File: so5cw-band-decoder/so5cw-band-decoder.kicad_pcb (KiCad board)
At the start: 2 copper layers, 140 x 154 mm, 136 parts, among them J1 DA15_Receptacle, J2 AudioJack3_SwitchTR, J3 Barrel_Jack_MountingPin, J4 RJ45, K1 TIANBO-HJR-4102-L, K10 TIANBO-HJR-4102-L, K11 TIANBO-HJR-4102-L, K12 TIANBO-HJR-4102-L, K2 TIANBO-HJR-4102-L, K3 TIANBO-HJR-4102-L, K4 TIANBO-HJR-4102-L, K5 TIANBO-HJR-4102-L, K6 TIANBO-HJR-4102-L, K7 TIANBO-HJR-4102-L, K8 TIANBO-HJR-4102-L, K9 TIANBO-HJR-4102-L, Q1 BS170F, Q2 BS170F, Q3 BS170F, Q4 BS170F, SW1 TASTER 3305D, SW2 TASTER 3305D, SW3 TASTER 3305D, SW4 TASTER 3305D, SW5 SW_Omron_B3FS, U1 RaspberryPi_Pico, U2 ULN2003A, U3 ULN2003A, U4 LM78M05_TO220

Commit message: Rearrange parts and route the critical connections. Needs cleanup.
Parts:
- C1, C10, C11, C12, C13, C14, C15, C16, C17, C18, C19, C2, C20, C21, C22, C23, C24, C3, C4, C5, C6, C7, C8, C9, R33: moved to B.Cu
- moved C30 90.7 mm to (148.6, 49.5)
- moved C31 87.2 mm to (148.3, 56.1)
- moved K1 84.6 mm to (46.0, 137.7)
- moved C29 82.6 mm to (81.5, 29.5), turned to 90 degrees
- moved K2 69.3 mm to (46.0, 121.9)
- moved K12 68.2 mm to (96.5, 150.4), turned to 180 degrees
- moved R17 68.0 mm to (101.2, 26.4), turned to 180 degrees
- moved R18 67.2 mm to (101.3, 29.0), turned to 180 degrees
- moved R19 65.9 mm to (123.7, 158.8), turned to 90 degrees
- moved K11 65.3 mm to (96.5, 134.9), turned to 180 degrees
- moved K3 56.7 mm to (46.0, 106.2)
- moved K10 53.6 mm to (96.5, 119.1), turned to 180 degrees
- moved K8 53.5 mm to (96.5, 87.9), turned to 180 degrees
- moved C6 51.7 mm to (73.2, 75.2)
- moved C5 50.1 mm to (71.4, 75.2)
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- renumbered K8 to K10, K10 to K11, K9 to K8, K11 to K9
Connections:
- R1 pad 2: /R1A -> /R1F
- R10 pad 2: /R2D -> /R2C
- R11 pad 2: /R2E -> /R2B
- R12 pad 2: /R2F -> /R2A
- R2 pad 2: /R1B -> /R1E
- R3 pad 2: /R1C -> /R1D
- R4 pad 2: /R1D -> /R1C
- R5 pad 2: /R1E -> /R1B
- R6 pad 2: /R1F -> /R1A
- R7 pad 2: /R2A -> /R2F
- R8 pad 2: /R2B -> /R2E
- R9 pad 2: /R2C -> /R2D
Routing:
- net +12V: track 0.00 -> 196.7 mm
- net /R2AR: track 0.00 -> 187.3 mm
- net /SW1: track 0.00 -> 175.2 mm
- net /SW2: track 0.00 -> 169.0 mm
- net /R1AR: track 0.00 -> 159.4 mm, vias 0 -> 1
- net /R2BR: track 0.00 -> 151.7 mm
- net /R1BR: track 0.00 -> 149.6 mm, vias 0 -> 1
- net /R1FR: track 0.00 -> 137.3 mm, vias 0 -> 1
- net /R1CR: track 0.00 -> 135.1 mm, vias 0 -> 1
- net /R2FP: track 0.00 -> 123.8 mm
- net /R1DR: track 0.00 -> 123.7 mm, vias 0 -> 1
- net /SW4: track 0.00 -> 121.6 mm
- net /R1ER: track 0.00 -> 119.3 mm, vias 0 -> 1
- net /R2CR: track 0.00 -> 117.6 mm
- net /SW3: track 0.00 -> 115.9 mm
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
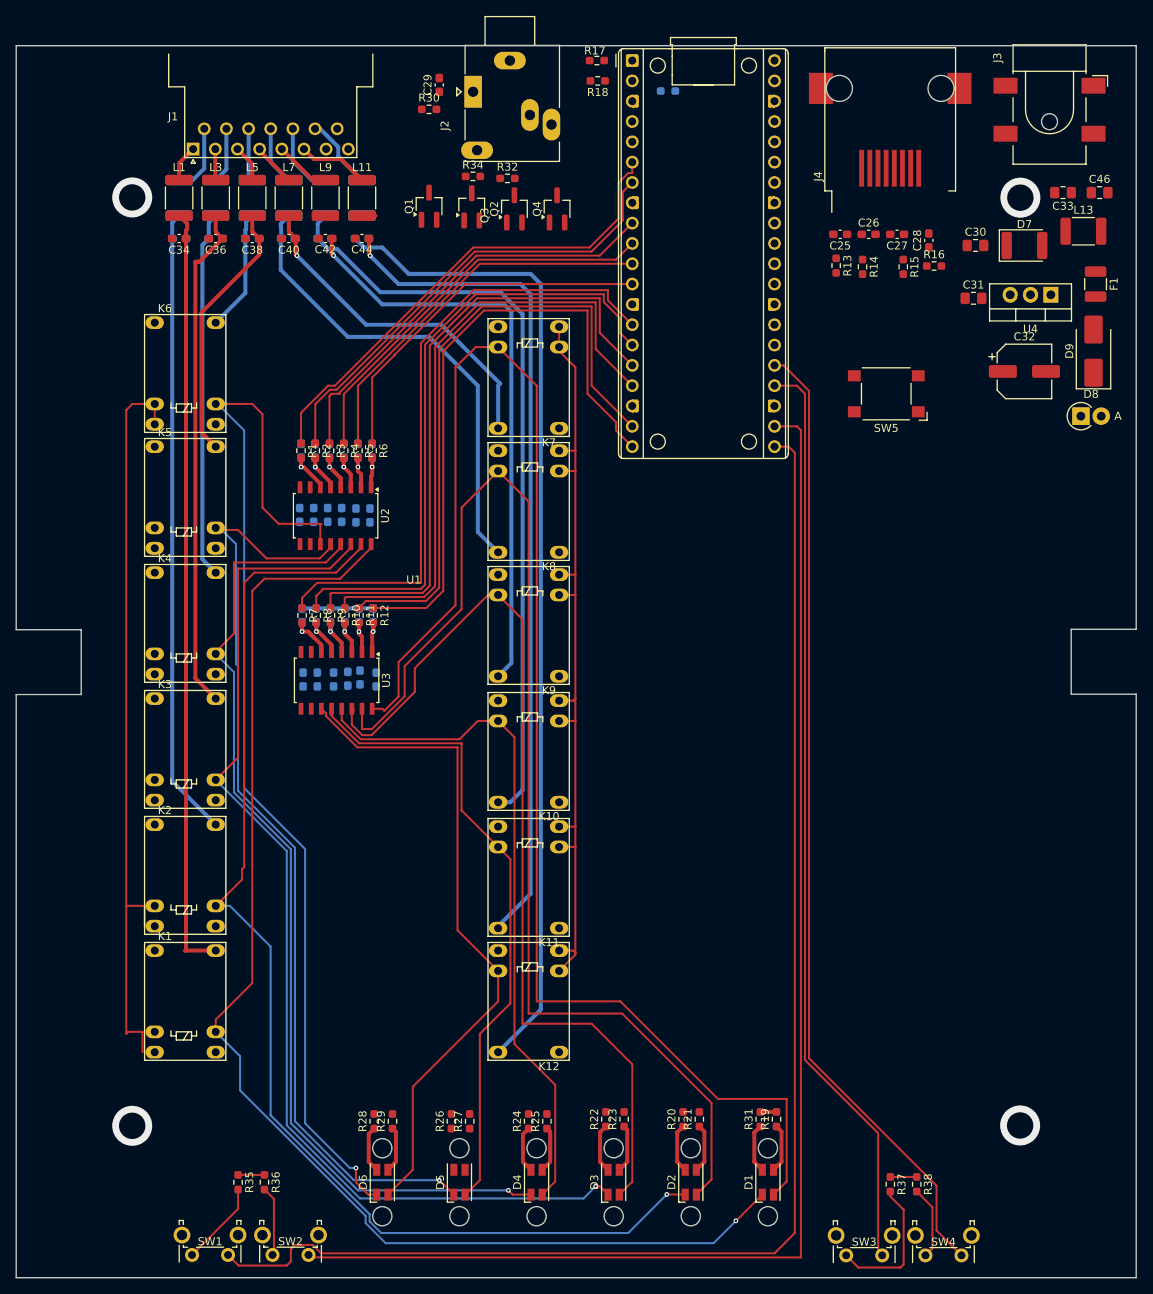
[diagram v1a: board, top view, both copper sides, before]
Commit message: some more routing, add buzzer, heatsink for 5V reg, etc.
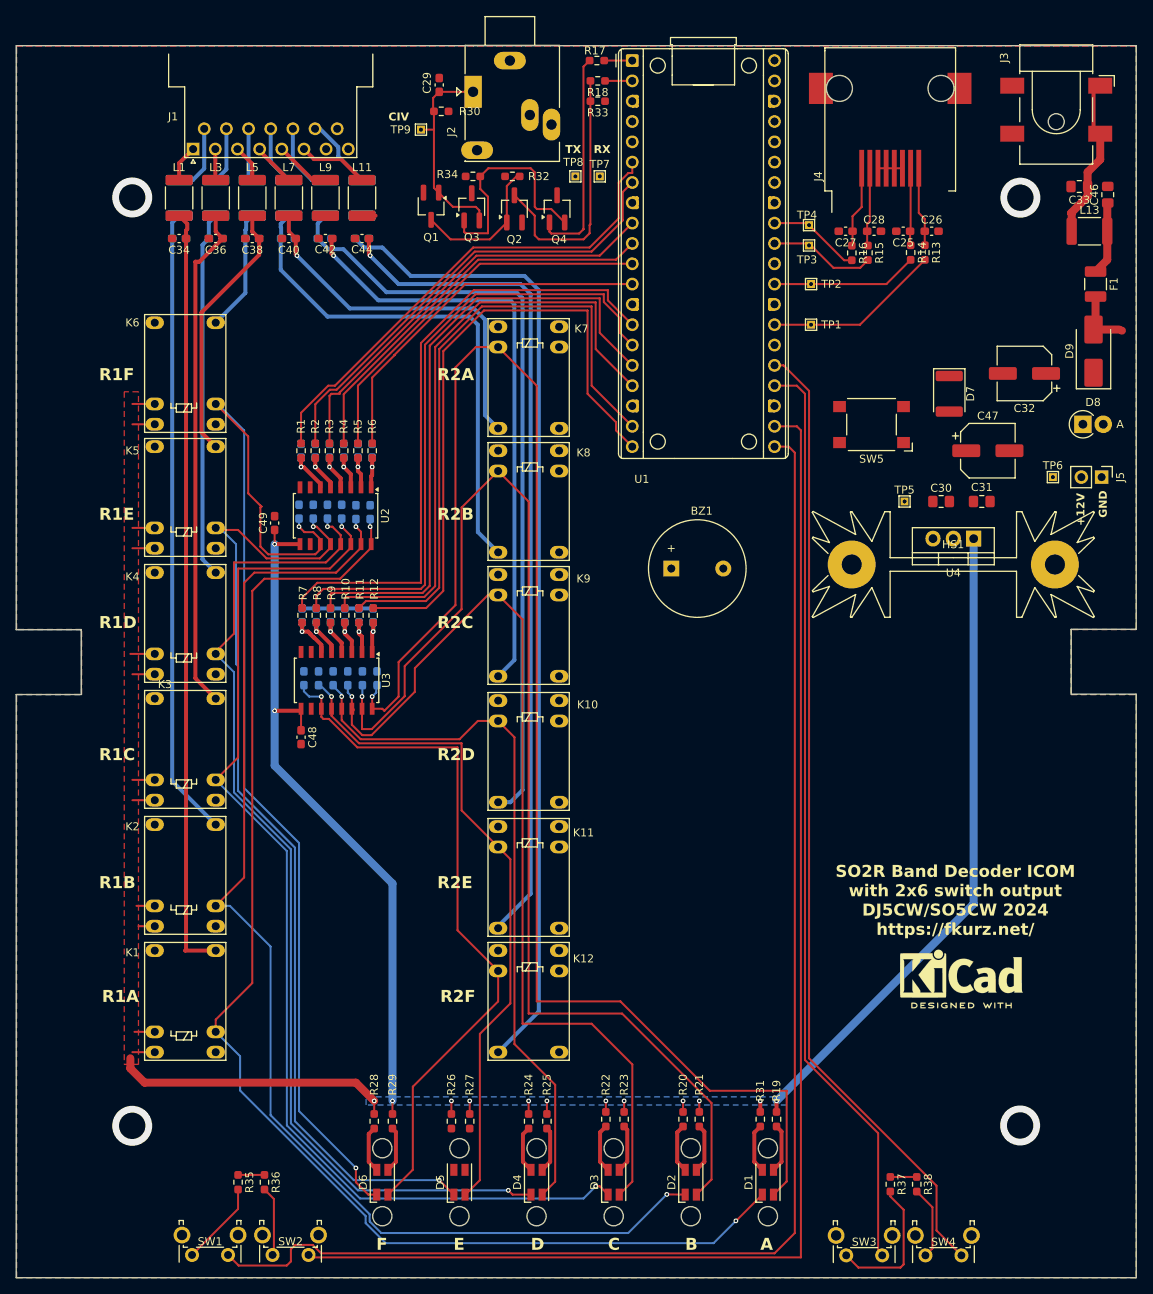
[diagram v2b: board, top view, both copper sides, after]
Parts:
- added BZ1: Buzzer, so5cw-band-decoder-components:Buzzer_12x9.5RM6.5, F.Cu at (110.5, 89.9)
- added C47: 47u, Capacitor_SMD:CP_Elec_6.3x7.7, F.Cu at (150.1, 75.2)
- added C48: 100n, Capacitor_SMD:C_0603_1608Metric_Pad1.08x0.95mm_HandSolder, F.Cu at (64.3, 111.0)
- added C49: 100n, Capacitor_SMD:C_0603_1608Metric_Pad1.08x0.95mm_HandSolder, F.Cu at (61.0, 84.2)
- added FID1: KiCad Logo, Symbol:KiCad-Logo2_6mm_SilkScreen, F.Cu at (146.8, 140.5)
- added HS1: Heatsink_Pad, Heatsink:Heatsink_Fischer_SK104-STC-STIC_35x13mm_2xDrill2.5mm, F.Cu at (145.8, 89.4)
- added J5: Conn_01x02_Pin, Connector_PinHeader_2.54mm:PinHeader_1x02_P2.54mm_Vertical, F.Cu at (164.3, 78.5)
- added TP1: TestPoint, TestPoint:TestPoint_THTPad_1.0x1.0mm_Drill0.5mm, F.Cu at (128.0, 59.4)
- added TP2: TestPoint, TestPoint:TestPoint_THTPad_1.0x1.0mm_Drill0.5mm, F.Cu at (128.0, 54.4)
- added TP3: TestPoint, TestPoint:TestPoint_THTPad_1.0x1.0mm_Drill0.5mm, F.Cu at (127.8, 49.5)
- added TP4: TestPoint, TestPoint:TestPoint_THTPad_1.0x1.0mm_Drill0.5mm, F.Cu at (127.8, 47.0)
- added TP5: TestPoint, TestPoint:TestPoint_THTPad_1.0x1.0mm_Drill0.5mm, F.Cu at (139.7, 81.5)
- added TP6: TestPoint, TestPoint:TestPoint_THTPad_1.0x1.0mm_Drill0.5mm, F.Cu at (158.2, 78.5)
- added TP7: TestPoint, TestPoint:TestPoint_THTPad_1.0x1.0mm_Drill0.5mm, F.Cu at (101.6, 40.9)
- added TP8: TestPoint, TestPoint:TestPoint_THTPad_1.0x1.0mm_Drill0.5mm, F.Cu at (98.6, 40.9)
- added TP9: TestPoint, TestPoint:TestPoint_THTPad_1.0x1.0mm_Drill0.5mm, F.Cu at (79.2, 35.1)
- J3: value Barrel_Jack_MountingPin -> Barrel_Jack
- R33: moved to F.Cu
- moved C30 32.3 mm to (144.3, 81.5)
- moved U4 32.0 mm to (148.3, 86.2)
- moved C31 25.4 mm to (149.4, 81.5)
- moved D7 20.8 mm to (145.3, 68.1), turned to -90 degrees
- moved R13 11.2 mm to (142.2, 50.4)
- moved R16 10.4 mm to (133.1, 50.5), turned to -90 degrees
- moved R33 8.88 mm to (101.3, 31.5)
- moved C26 7.88 mm to (143.1, 47.8)
- moved C25 7.88 mm to (139.5, 47.8)
- moved C28 6.94 mm to (135.9, 47.8), turned to 0 degrees
- moved C27 6.45 mm to (132.3, 47.8)
- moved R14 6.27 mm to (140.5, 50.4)
- moved R15 4.74 mm to (135.1, 50.4)
- moved SW5 4.26 mm to (135.6, 71.9)
- moved C33 2.17 mm to (161.5, 42.2)
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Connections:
- J4 pad 1: /R1_TX -> /R1_BAND
- J4 pad 2: /R2_TX -> /R2_BAND
- J4 pad 7: /R1_BAND -> /R1_TX
- J4 pad 8: /R2_BAND -> /R2_TX
- R13 pad 1: /R1_TX -> /R2_TX
- R14 pad 1: /R2_TX -> /R1_TX
- R15 pad 1: /R1_BAND -> /R2_BAND
- R16 pad 1: /R2_BAND -> /R1_BAND
- U1 pad 5: unconnected-(U1-GPIO3-Pad5) -> /BUZZER
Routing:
- net +12V: track 196.7 -> 259.1 mm, vias 0 -> 14
- net /UART_RX: track 0.00 -> 32.5 mm
- net Net-(Q3-G): track 0.00 -> 28.3 mm
- net /UART_TX: track 0.00 -> 27.1 mm
- net Net-(Q1-G): track 0.00 -> 26.8 mm
- net Net-(U1-GPIO21): track 0.00 -> 22.2 mm
- net Net-(C33-Pad1): track 0.00 -> 19.7 mm
- net Net-(U1-GPIO22): track 0.00 -> 18.3 mm
- net Net-(Q1-D): track 0.00 -> 18.0 mm
- net Net-(U1-GPIO26_ADC0): track 0.00 -> 13.3 mm
- net Net-(U1-GPIO27_ADC1): track 0.00 -> 11.6 mm
- net /R2_BAND: track 0.00 -> 10.6 mm
- net /R2_TX: track 0.00 -> 10.3 mm
- net /R1_BAND: track 0.00 -> 10.2 mm
- net /R1_TX: track 0.00 -> 9.68 mm
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- added copper zone on B.Cu, net +12V
- added copper zone on F.Cu, net +12V
- added copper zone on B.Cu, net GND
- added copper zone on F.Cu, net GND
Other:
- board text added: "+12V"
- board text added: "A"
- board text added: "B"
- board text added: "C"
- board text added: "CIV"
- board text added: "D"
- board text added: "E"
- board text added: "F"
- board text added: "GND"
- board text added: "R1A"
- board text added: "R1B"
- board text added: "R1C"
- board text added: "R1D"
- board text added: "R1E"
- board text added: "R1F"
- board text added: "R2A"
- board text added: "R2B"
- board text added: "R2C"
- board text added: "R2D"
- board text added: "R2E"
- board text added: "R2F"
- board text added: "RX"
- board text added: "SO2R Band Decoder ICOM with 2x6 switch output DJ5CW/SO5CW 2024 https://fkurz.net/"
- board text added: "TX"
